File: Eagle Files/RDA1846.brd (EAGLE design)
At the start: 80 x 80 mm, 1 part

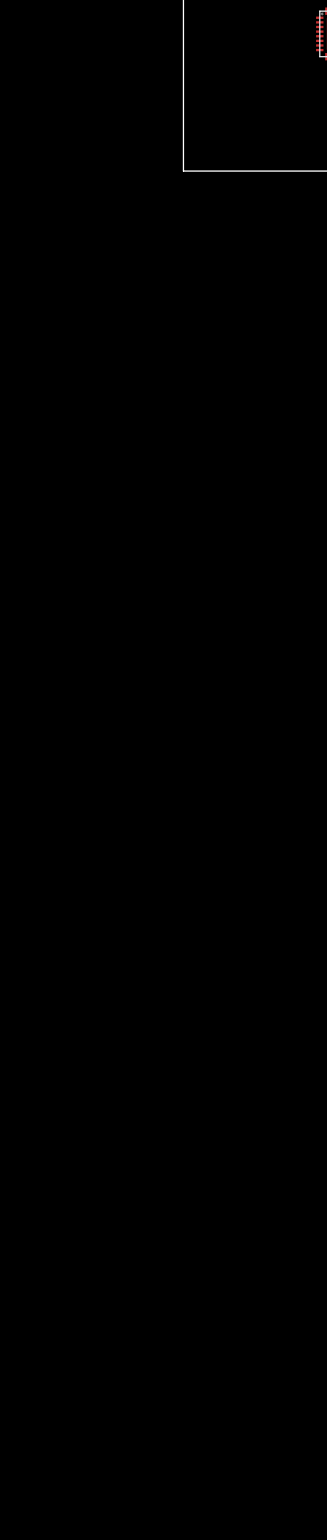
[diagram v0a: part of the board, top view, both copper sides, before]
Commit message: Added FA-128 XTAL Library. WIP : Schematic
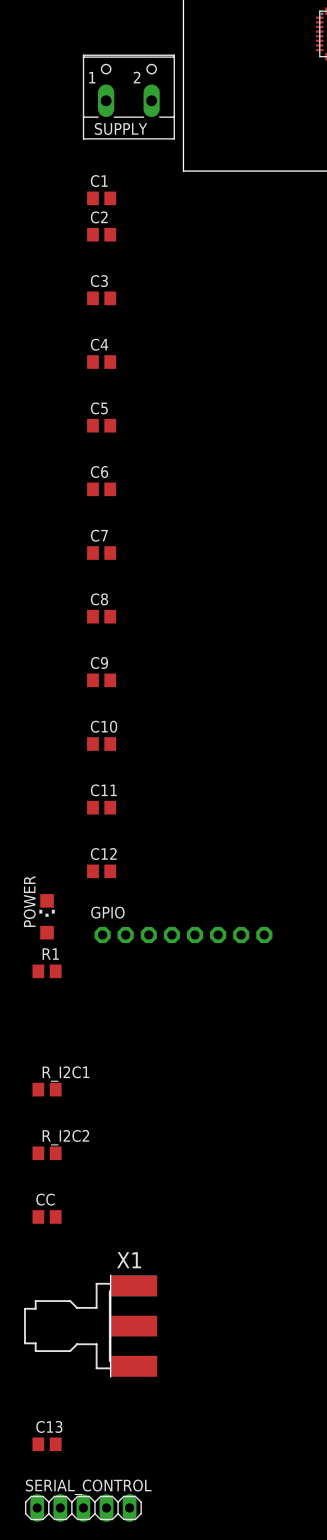
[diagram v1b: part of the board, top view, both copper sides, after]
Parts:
- added C1, C11, C13, C3, C5, C7, C9: 100nF, rcl:C0805
- added C10, C12, C2, C4, C6, C8: 1nF, rcl:C0805
- added CC: 47uF, rcl:C0805
- added GPIO: (no value), adafruit:1X08-CLEANBIG
- added POWER: (no value), adafruit:CHIPLED_1206
- added R1: 1K, rcl:R0805
- added R_I2C1, R_I2C2: 10K, rcl:R0805
- added SERIAL_CONTROL: (no value), pinhead:1X05
- added SUPPLY: (no value), con-wago-500:W237-102
- added X1: SMA-142-0701-851/861, con-coax:J502-ND-142-0701-851/861
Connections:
- new net GND: C1.2, C10.2, C11.2, C12.2, C2.2, C3.2, C4.2, C5.2, C6.2, C7.2, C8.2, C9.2, CC.2, R1.2, SERIAL_CONTROL.1, SUPPLY.2, U$1.PAD, X1.G@1, X1.G@2, X1.G@3, X1.G@4
- new net MODE: SERIAL_CONTROL.3, U$1.MODE
- new net N$1: GPIO.1, U$1.GPIO0
- new net N$10: CC.1, U$1.CC
- new net N$11: C13.1, U$1.NC@4
- new net N$12: C13.2, X1.1
- new net N$2: GPIO.8, U$1.GPIO7
- new net N$3: GPIO.2, U$1.GPIO1
- new net N$4: GPIO.7, U$1.GPIO6
- new net N$5: GPIO.3, U$1.GPIO2
- new net N$6: GPIO.6, U$1.GPIO5
- new net N$7: GPIO.4, U$1.GPIO3
- new net N$8: GPIO.5, U$1.GPIO4
- new net N$9: POWER.C, R1.1
- new net PABIAS: U$1.PABIAS
- new net SCLK: R_I2C1.1, SERIAL_CONTROL.5, U$1.SCLK
- new net SDIO: R_I2C2.1, SERIAL_CONTROL.4, U$1.SDIO
- new net SENB: SERIAL_CONTROL.2, U$1.SENB
- new net VDD: C1.1, C10.1, C11.1, C12.1, C2.1, C3.1, C4.1, C5.1, C6.1, C7.1, C8.1, C9.1, POWER.A, R_I2C1.2, R_I2C2.2, SUPPLY.1, U$1.AVDD@1, U$1.AVDD@2, U$1.AVDD@3, U$1.AVDD@4, U$1.AVDD@5, U$1.AVDD@6

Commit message: Schematics done. Layout WIP. Check RF Switch dimensions
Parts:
- added AOUT, MIC: (no value), pinhead:1X02
- added C14, C15: 9pF, rcl:C0805
- added C16, C17: 47uF, rcl:C0805
- added C18, C19, C20: (no value), rcl:C1206
- added ENABLE, RF_SWITCH: (no value), pinhead:1X03
- added PABIAS: (no value), con-wago-500:W237-102
- added RFIN, RFOUT: SMA-142-0701-851/861, con-coax:J502-ND-142-0701-851/861
- added U$2: CRYSTAL_FA_128, FA_128:FA_128
- added U$3: RF_SWITCH, RF_SWITCH:SC90
- added X2, X3: SMA-142-0701-871/876, con-coax:J502-ND-142-0701-871/876
- X1: value SMA-142-0701-851/861 -> SMA-142-0701-871/876; device con-coax:J502-ND-142-0701-851/861 -> con-coax:J502-ND-142-0701-871/876
- moved X1 154.6 mm to (-30.0, -280.0)
- moved SUPPLY 11.5 mm to (1.31, 17.9), turned to 90 degrees
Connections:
- new net N$13: C15.1, U$1.XTAL1, U$2.P$3
- new net N$14: C14.1, U$1.XTAL2, U$2.P$1
- new net N$15: C16.2, U$1.AFOUT
- new net N$16: C17.2, U$1.MIC_IN
- new net N$17: AOUT.2, C16.1
- new net N$18: C17.1, MIC.2
- new net N$19: RFIN.1, U$1.RFIN
- new net N$20: C19.2, X1.1
- new net N$21: C19.1, U$3.P$1
- new net N$22: C20.1, U$3.P$3
- new net N$23: C20.2, X2.1
- new net N$24: C18.1, U$3.P$5
- new net N$25: C18.2, X3.1
- new net N$26: RF_SWITCH.2, U$3.P$4
- new net N$27: RF_SWITCH.3, U$3.P$6
- new net PDN: ENABLE.2, U$1.PDN
- net GND: now also AOUT.1, C14.2, C15.2, ENABLE.1, MIC.1, PABIAS.2, RFIN.G@1, RFIN.G@2, RFIN.G@3, RFIN.G@4, RFOUT.G@1, RFOUT.G@2, RFOUT.G@3, RFOUT.G@4, RF_SWITCH.1, U$2.P$2, U$2.P$4, U$3.P$2, X2.G@1, X2.G@2, X2.G@3, X2.G@4
- net N$11: now also U$1.RF_OUT; no longer U$1.NC@4
- net N$12: now also RFOUT.1; no longer X1.1
- net PABIAS: now also PABIAS.1
- net VDD: now also ENABLE.3
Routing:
- added copper zone on layer 1, net GND
- added copper zone on layer 16, net GND

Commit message: Placing of component done. Removed demod spec due to size constraints
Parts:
- removed AOUT: (no value), pinhead:1X02
- removed C16: 47uF, rcl:C0805
- removed PABIAS: (no value), con-wago-500:W237-102
- removed RFIN: SMA-142-0701-851/861, con-coax:J502-ND-142-0701-851/861
- removed RF_SWITCH: (no value), pinhead:1X03
- removed SERIAL_CONTROL: (no value), pinhead:1X05
- added JP1: (no value), pinhead:1X02
- added JP2, JP3: (no value), pinhead:1X03
- added JP4, JP5, JP6: (no value), pinhead:1X01
- moved X3 362.5 mm to (57.3, 31.9), turned to 270 degrees
- moved X2 333.9 mm to (69.2, 18.8), turned to 180 degrees
- moved C20 302.9 mm to (61.1, 18.8)
- moved X1 299.2 mm to (57.3, 6.17), turned to 90 degrees
- moved C18 287.6 mm to (57.3, 24.1), turned to 90 degrees
- moved C19 287.6 mm to (57.3, 14.0), turned to 270 degrees
- moved U$3 265.6 mm to (55.1, 18.0)
- moved ENABLE 245.4 mm to (42.8, 29.7)
- moved C17 207.4 mm to (26.0, 16.2), turned to 90 degrees
- moved MIC 189.2 mm to (26.0, 11.0), turned to 90 degrees
- moved C15 186.1 mm to (21.8, 21.3), turned to 180 degrees
- moved C14 172.8 mm to (21.3, 14.8), turned to 270 degrees
- moved U$2 169.5 mm to (21.3, 18.1)
- moved C13 163.7 mm to (43.4, 12.9), turned to 270 degrees
- moved RFOUT 142.4 mm to (43.5, 5.72), turned to 90 degrees
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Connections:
- removed net N$15: C16.2, U$1.AFOUT
- removed net N$17: AOUT.2, C16.1
- removed net N$19: RFIN.1, U$1.RFIN
- net GND: now also JP1.1, JP2.1, JP3.1, JP4.1, SUPPLY.1; no longer AOUT.1, PABIAS.2, RFIN.G@1, RFIN.G@2, RFIN.G@3, RFIN.G@4, RF_SWITCH.1, SERIAL_CONTROL.1, SUPPLY.2
- net MODE: now also JP3.3; no longer SERIAL_CONTROL.3
- net N$26: now also JP5.1; no longer RF_SWITCH.2
- net N$27: now also JP6.1; no longer RF_SWITCH.3
- net PABIAS: now also JP1.2; no longer PABIAS.1
- net SCLK: now also JP2.3; no longer SERIAL_CONTROL.5
- net SDIO: now also JP2.2; no longer SERIAL_CONTROL.4
- net SENB: now also JP3.2; no longer SERIAL_CONTROL.2
- net VDD: now also SUPPLY.2; no longer SUPPLY.1
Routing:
- net VDD: track 0.00 -> 37.9 mm
- net N$2: track 0.00 -> 9.27 mm
- net N$1: track 0.00 -> 9.24 mm
- net N$4: track 0.00 -> 7.55 mm
- net N$3: track 0.00 -> 7.51 mm
- net N$6: track 0.00 -> 5.86 mm
- net N$5: track 0.00 -> 5.85 mm
- net N$8: track 0.00 -> 5.02 mm
- net N$7: track 0.00 -> 5.01 mm
- net N$9: track 0.00 -> 2.24 mm
- net GND: track 0.00 -> 1.39 mm, vias 0 -> 4
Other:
- board size 80 x 80 mm -> 69.4 x 26.1 mm

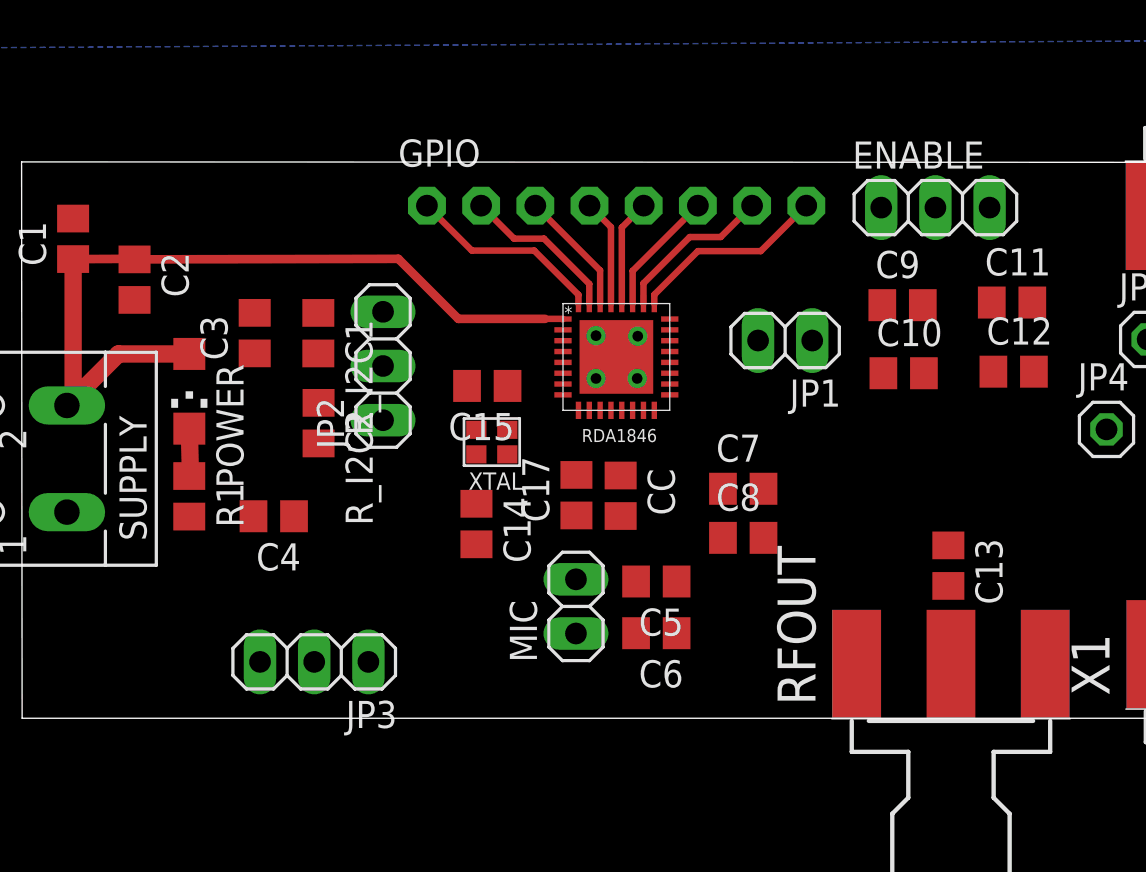
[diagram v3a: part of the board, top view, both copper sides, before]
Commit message: Layout RDA almost done. VCC lines remaining
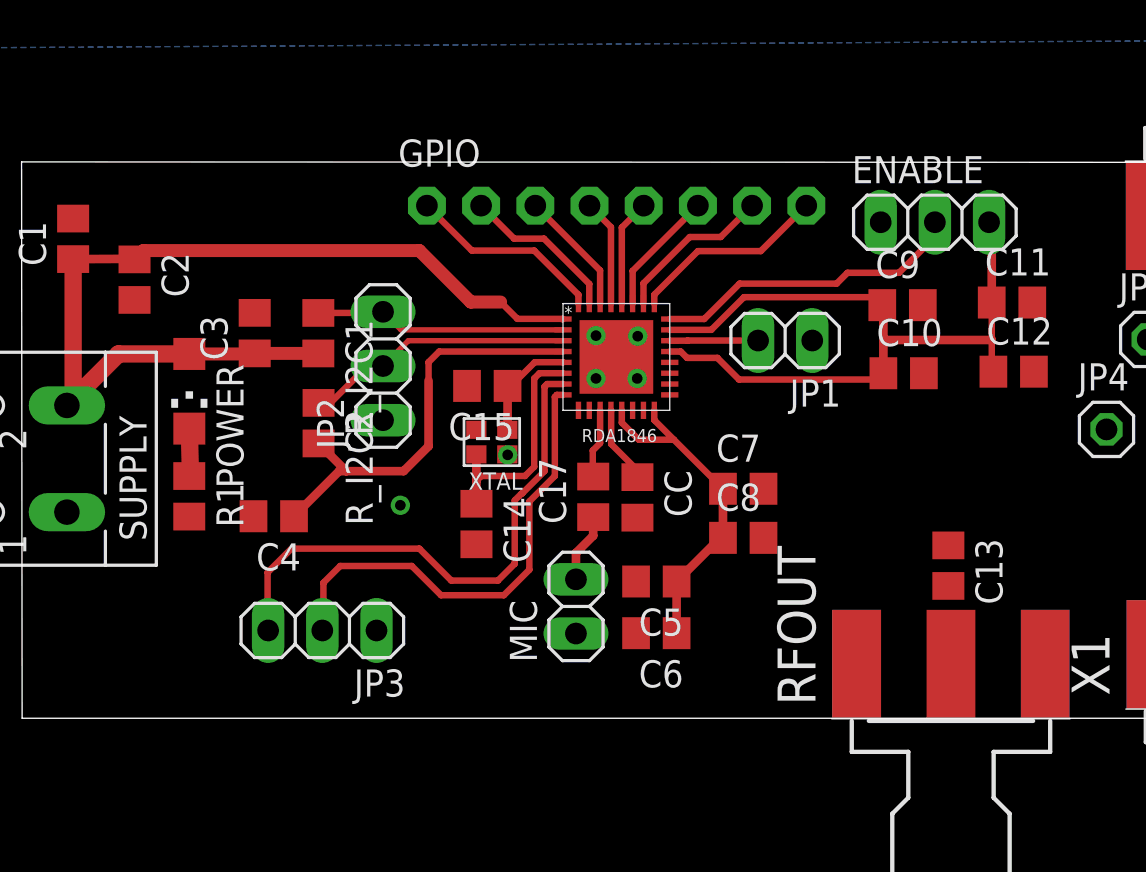
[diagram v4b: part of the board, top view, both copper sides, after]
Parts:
- moved JP3 1.52 mm to (14.1, 9.86)
- moved C17 0.79 mm to (26.8, 16.1)
- moved CC 0.79 mm to (28.8, 16.1)
- moved ENABLE 0.69 mm to (42.8, 29.0)
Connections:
- net GND: now also X3.G@1, X3.G@2, X3.G@3, X3.G@4
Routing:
- net VDD: track 37.9 -> 117.2 mm
- net MODE: track 0.00 -> 25.5 mm
- net SENB: track 0.00 -> 22.3 mm
- net PDN: track 0.00 -> 14.7 mm
- net SDIO: track 0.00 -> 12.7 mm
- net SCLK: track 0.00 -> 11.8 mm
- net N$14: track 0.00 -> 10.9 mm
- net N$13: track 0.00 -> 5.12 mm
- net PABIAS: track 0.00 -> 4.14 mm
- net N$10: track 0.00 -> 3.64 mm
- net N$16: track 0.00 -> 3.26 mm
- net N$18: track 0.00 -> 3.25 mm
- net GND: track 1.39 -> 1.42 mm, vias 4 -> 6

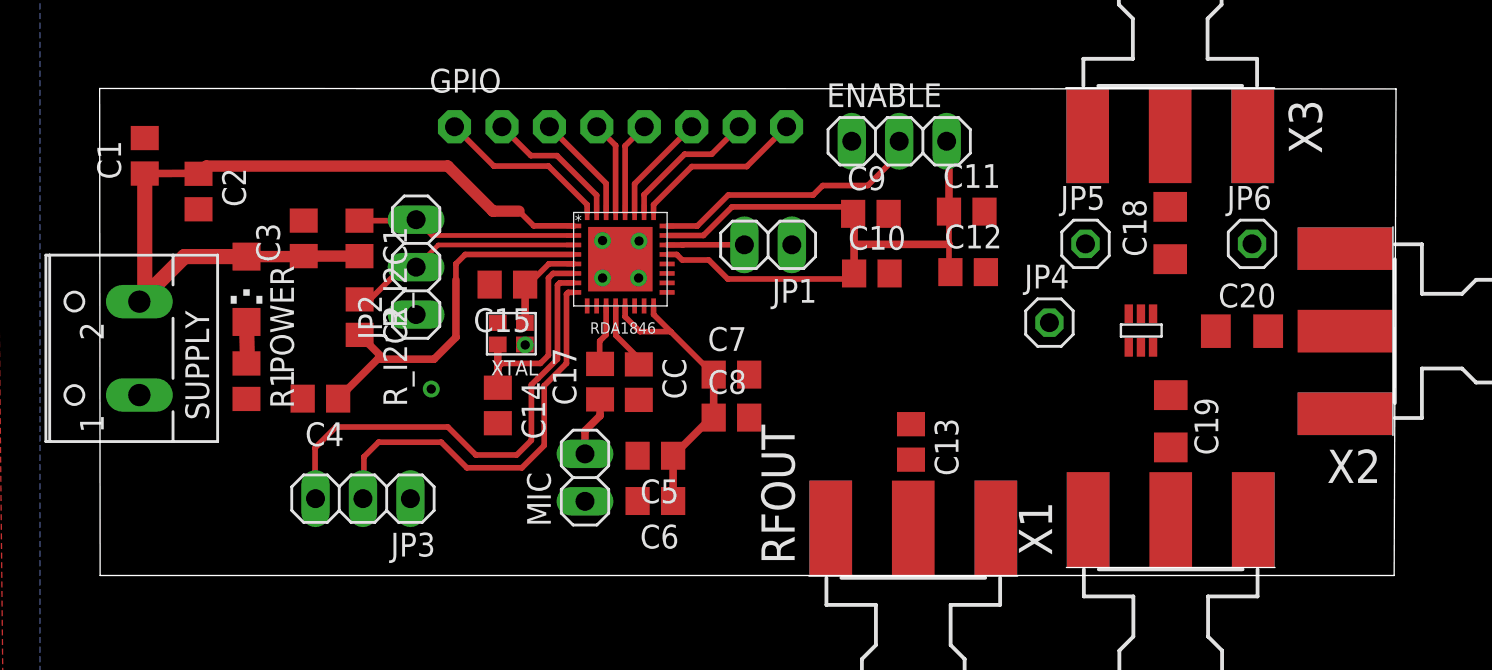
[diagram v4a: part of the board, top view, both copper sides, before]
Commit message: Completed layout and routing. Need to adjust labels and values
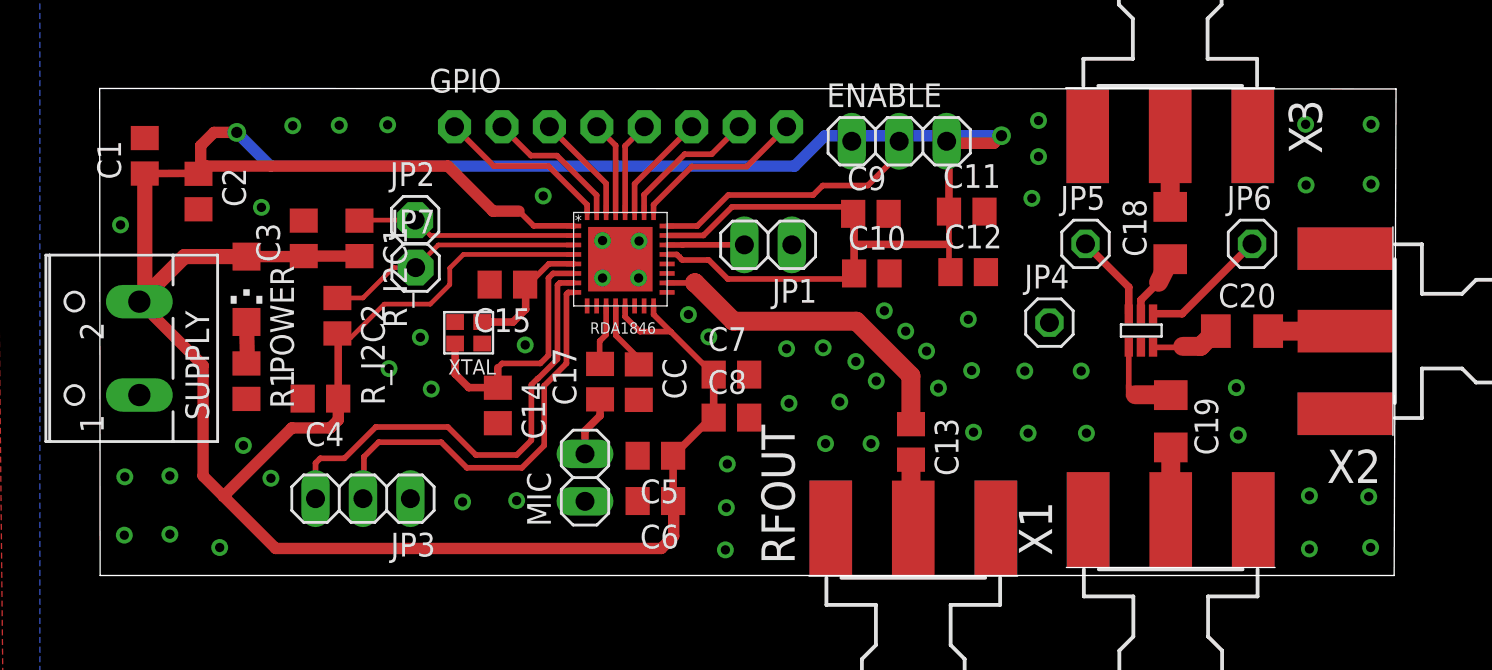
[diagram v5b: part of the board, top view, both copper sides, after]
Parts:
- added JP7: (no value), adafruit:1X01
- JP2: device pinhead:1X03 -> adafruit:1X01
- moved JP2 2.52 mm to (16.9, 24.8), turned to 0 degrees
- moved U$2 2.29 mm to (19.0, 18.2)
- moved R_I2C2 1.20 mm to (12.7, 19.6)
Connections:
- net GND: no longer JP2.1
- net SCLK: now also JP2.1; no longer JP2.3
- net SDIO: now also JP7.1; no longer JP2.2
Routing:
- net VDD: track 117.2 -> 253.6 mm, vias 0 -> 2
- net N$11: track 0.00 -> 17.7 mm
- net N$27: track 0.00 -> 6.85 mm
- net N$26: track 0.00 -> 4.70 mm
- net N$21: track 0.00 -> 4.59 mm
- net N$23: track 0.00 -> 4.12 mm
- net N$20: track 0.00 -> 3.86 mm
- net N$25: track 0.00 -> 3.81 mm
- net N$22: track 0.00 -> 3.72 mm
- net N$12: track 0.00 -> 3.71 mm
- net N$24: track 0.00 -> 3.46 mm
- net N$14: track 10.9 -> 13.9 mm
- net N$13: track 5.12 -> 7.01 mm
- net SDIO: track 12.7 -> 13.8 mm
- net GND: vias 6 -> 60

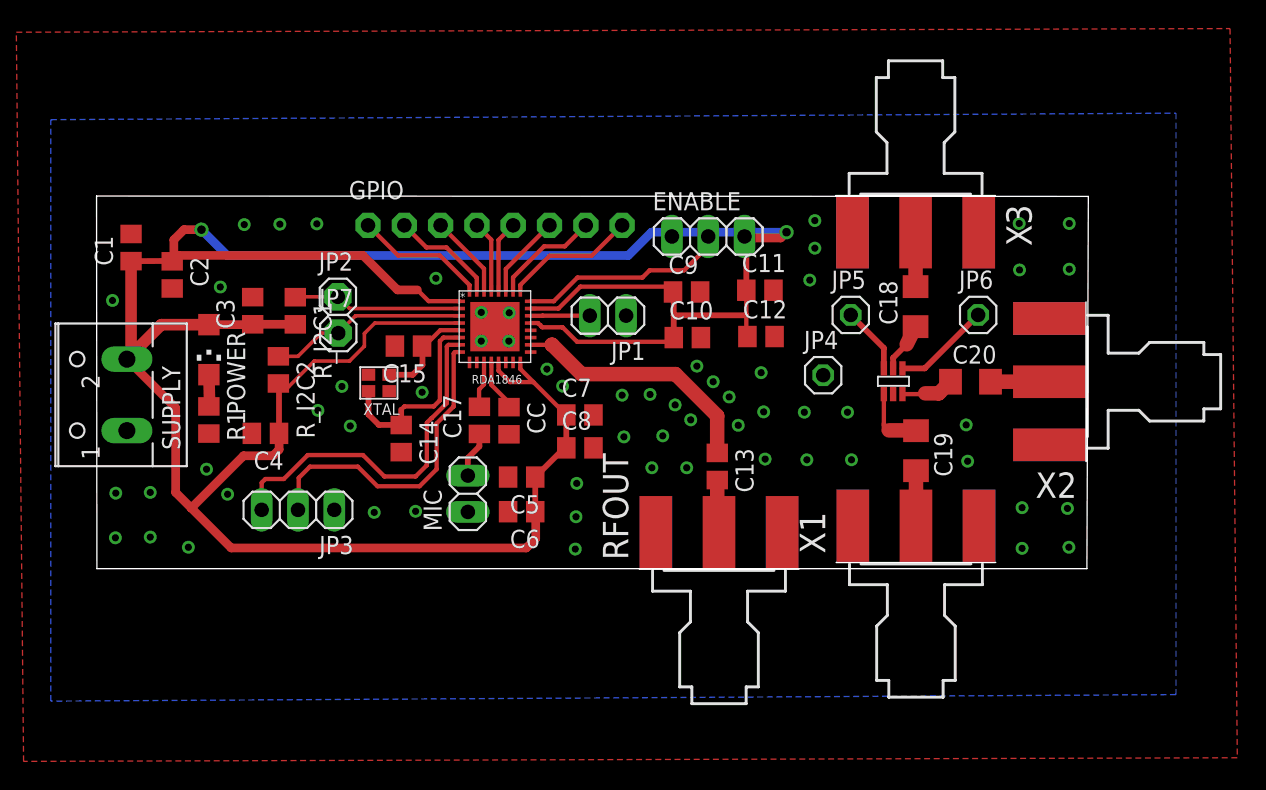
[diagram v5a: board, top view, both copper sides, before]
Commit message: Placed all the names and values. QA remaining
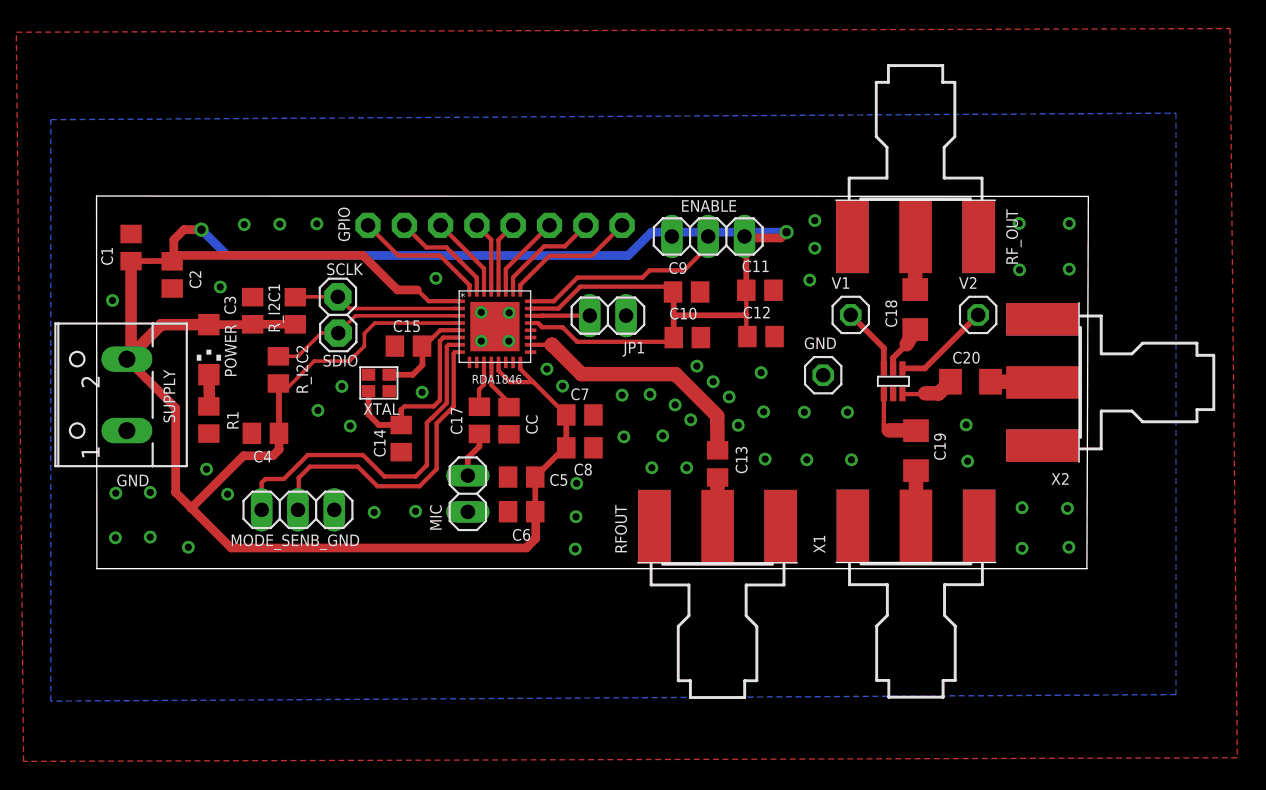
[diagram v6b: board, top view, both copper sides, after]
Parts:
- removed X3: SMA-142-0701-871/876, con-coax:J502-ND-142-0701-871/876
- added RF_OUT: SMA-142-0701-871/876, con-coax:J502-ND-142-0701-871/876
- moved X2 0.49 mm to (68.7, 18.8)
- moved RFOUT 0.44 mm to (43.4, 6.15)
- moved C18 0.20 mm to (57.3, 23.9)
- moved C13 0.18 mm to (43.4, 13.1)
- renumbered JP2 to SCLK, JP3 to MODE_SENB_GND, JP4 to GND, JP5 to V1, JP6 to V2, JP7 to SDIO
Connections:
- net GND: now also RF_OUT.G@1, RF_OUT.G@2, RF_OUT.G@3, RF_OUT.G@4; no longer X3.G@1, X3.G@2, X3.G@3, X3.G@4
- net N$25: now also RF_OUT.1; no longer X3.1
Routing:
- net N$12: track 3.71 -> 4.27 mm
- net N$25: track 3.81 -> 4.34 mm
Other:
- board text added: "GND"
